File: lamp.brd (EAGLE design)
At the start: 127.3 x 38.1 mm, 53 parts

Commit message: Fiddled the board xml by hand to place the last few parts. Some more adjustment of traces. Added a low-noise cap to the 5v regulator.
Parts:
- added C3: 10nF, Barebones-Arduino:0805
- C1: value (none) -> 1µF
- C2: value (none) -> 2.2µF
- moved C2 1.62 mm to (67.3, 4.13), turned to 180 degrees
- moved C1 1.27 mm to (58.7, 5.71)
- moved LR 1.27 mm to (62.2, 5.71)
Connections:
- new net N$46: C3.1, LR.P$4
- net GND: now also C3.2
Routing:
- net N$15: track 14.1 -> 22.4 mm
- net N$46: track 0.00 -> 2.99 mm
- net GND: vias 8 -> 10
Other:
- board text added: "C1"
- board text added: "C2"
- board text added: "C3"
- board text added: "LR"
- board text added: "R1"
- board text added: "R10"
- board text added: "R2"
- board text added: "R3"
- board text added: "R4"
- board text added: "R5"
- board text added: "R6"
- board text added: "R7"
- board text added: "R8"
- board text added: "R9"
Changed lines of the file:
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@@
 <rectangle x1="120.9675" y1="30.1625" x2="124.46" y2="32.7025" layer="1"/>
 <rectangle x1="120.9675" y1="33.3375" x2="124.46" y2="35.8775" layer="1"/>
+<text x="62.23" y="3.81" size="1.016" layer="26" rot="MR0" align="top-center">LR</text>
+<text x="57.785" y="5.715" size="1.016" layer="26" rot="MR0" align="center-left">C1</text>
+<text x="69.215" y="6.35" size="1.016" layer="26" rot="MR0" align="center-right">C3</text>
+<text x="69.215" y="4.1275" size="1.016" layer="26" rot="MR0" align="center-right">C2</text>
+<text x="10.795" y="34.925" size="1.016" layer="26" rot="MR180" align="top-center">R10</text>
+<text x="23.495" y="34.925" size="1.016" layer="26" rot="MR180" align="top-center">R9</text>
+<text x="36.195" y="34.925" size="1.016" layer="26" rot="MR180" align="top-center">R8</text>
+<text x="48.895" y="34.925" size="1.016" layer="26" rot="MR180" align="top-center">R7</text>
+<text x="61.595" y="34.925" size="1.016" layer="26" rot="MR180" align="top-center">R6</text>
+<text x="65.405" y="34.925" size="1.016" layer="26" rot="MR180" align="top-center">R5</text>
+<text x="78.105" y="34.925" size="1.016" layer="26" rot="MR180" align="top-center">R4</text>
+<text x="90.805" y="34.925" size="1.016" layer="26" rot="MR180" align="top-center">R3</text>
+<text x="103.505" y="34.925" size="1.016" layer="26" rot="MR180" align="top-center">R2</text>
+<text x="116.205" y="34.925" size="1.016" layer="26" rot="MR180" align="top-center">R1</text>
 </plain>
 <attributes>
@@
 <element name="U$17" library="lamp" package="PLCC4" value="CLA1BWKWMKW-4" x="57.15" y="19.05" rot="R90"/>
 <element name="U$18" library="lamp" package="PLCC4" value="CLA1BWKWMKW-4" x="57.15" y="33.02" rot="R90"/>
-<element name="LR" library="lamp" package="SOT-23-5" value="LP2985" x="63.5" y="5.715" smashed="yes" rot="MR90"/>
-<element name="C1" library=" Barebones-Arduino" package="0805" value="" x="60.0075" y="5.715" rot="MR90"/>
-<element name="C2" library=" Barebones-Arduino" package="0805" value="" x="66.9925" y="5.715" rot="MR90"/>
+<element name="LR" library="lamp" package="SOT-23-5" value="LP2985" x="62.23" y="5.715" smashed="yes" rot="MR90"/>
+<element name="C1" library=" Barebones-Arduino" package="0805" value="1µF" x="58.7375" y="5.715" rot="MR90"/>
+<element name="C2" library=" Barebones-Arduino" package="0805" value="2.2µF" x="67.31" y="4.1275" rot="MR180"/>
 <element name="PB1" library="wirepad" package="SMD1,27-2,54" value="" x="73.3425" y="11.7475" smashed="yes" rot="MR270">
 <attribute name="VALUE" x="73.3425" y="11.7475" size="0.0254" layer="28" rot="MR270"/>
@@
 <attribute name="NAME" x="51.6125" y="13.1825" size="1.27" layer="26" rot="MR0"/>
 </element>
+<element name="C3" library=" Barebones-Arduino" package="0805" value="10nF" x="67.31" y="6.35" rot="MR180"/>
 </elements>
 <signals>
@@
 <contactref element="LR" pad="P$1"/>
 <via x="63.5" y="1.27" extent="1-16" drill="0.5"/>
-<wire x1="63.5" y1="4.7625" x2="63.5" y2="6.0325" width="0.4064" layer="16"/>
-<wire x1="63.5" y1="6.0325" x2="62.865" y2="6.6675" width="0.4064" layer="16"/>
-<wire x1="62.865" y1="6.6675" x2="62.23" y2="6.6675" width="0.4064" layer="16"/>
-<wire x1="63.5" y1="1.27" x2="63.5" y2="4.7625" width="0.4064" layer="16"/>
-<wire x1="63.5" y1="4.7625" x2="60.0075" y2="4.7625" width="0.4064" layer="16"/>
+<wire x1="62.23" y1="4.7625" x2="62.23" y2="6.0325" width="0.4064" layer="16"/>
+<wire x1="62.23" y1="6.0325" x2="61.595" y2="6.6675" width="0.4064" layer="16"/>
+<wire x1="61.595" y1="6.6675" x2="60.96" y2="6.6675" width="0.4064" layer="16"/>
+<wire x1="63.5" y1="1.27" x2="62.23" y2="4.7625" width="0.4064" layer="16"/>
+<wire x1="62.23" y1="4.7625" x2="58.7375" y2="4.7625" width="0.4064" layer="16"/>
 <wire x1="121.6025" y1="1.27" x2="121.6025" y2="4.1275" width="1.27" layer="1"/>
 <wire x1="108.9025" y1="4.1275" x2="108.9025" y2="1.5875" width="1.27" layer="1"/>
 <wire x1="83.5025" y1="40.9575" x2="96.2025" y2="40.9575" width="0" layer="19" extent="1-1"/>
 <wire x1="63.5" y1="22.86" x2="83.5025" y2="40.9575" width="0" layer="19" extent="1-16"/>
-<wire x1="62.18" y1="6.635" x2="62.23" y2="6.6675" width="0" layer="19" extent="16-16"/>
-<wire x1="60.0075" y1="4.865" x2="60.0075" y2="4.7625" width="0" layer="19" extent="16-16"/>
-<wire x1="62.18" y1="4.795" x2="63.5" y2="4.7625" width="0" layer="19" extent="16-16"/>
+<wire x1="60.91" y1="6.635" x2="60.96" y2="6.6675" width="0" layer="19" extent="16-16"/>
+<wire x1="58.7375" y1="4.865" x2="58.7375" y2="4.7625" width="0" layer="19" extent="16-16"/>
+<wire x1="60.91" y1="4.795" x2="62.23" y2="4.7625" width="0" layer="19" extent="16-16"/>
 <wire x1="108.9025" y1="4.1275" x2="121.6025" y2="4.1275" width="0" layer="19" extent="1-1"/>
 <wire x1="96.2025" y1="3.4925" x2="83.5025" y2="3.4925" width="0" layer="19" extent="1-1"/>
@@
 <vertex x="127" y="0"/>
 </polygon>
-<wire x1="60.0075" y1="6.35" x2="60.96" y2="6.35" width="0.4064" layer="16"/>
-<wire x1="60.96" y1="6.35" x2="61.2775" y2="5.715" width="0.4064" layer="16"/>
-<wire x1="61.2775" y1="5.715" x2="62.23" y2="5.715" width="0.4064" layer="16"/>
-<polygon width="0" layer="1" spacing="0.254">
+<wire x1="58.7375" y1="6.35" x2="59.69" y2="6.35" width="0.4064" layer="16"/>
+<wire x1="59.69" y1="6.35" x2="60.0075" y2="5.715" width="0.4064" layer="16"/>
+<wire x1="60.0075" y1="5.715" x2="60.96" y2="5.715" width="0.4064" layer="16"/>
+<polygon width="0" layer="1" spacing="0.254" isolate="0.4064">
 <vertex x="0" y="0"/>
 <vertex x="127" y="0"/>
@@
 <via x="101.6" y="19.05" extent="1-16" drill="0.5"/>
 <via x="114.3" y="19.05" extent="1-16" drill="0.5"/>
+<contactref element="C3" pad="2"/>
+<via x="1.905" y="19.05" extent="1-16" drill="0.5"/>
+<via x="125.4125" y="19.05" extent="1-16" drill="0.5"/>
 </signal>
 <signal name="N$14">
@@
 </signal>
 <signal name="N$15">
-<wire x1="64.77" y1="4.7625" x2="68.58" y2="4.7625" width="0.4064" layer="16"/>
+<wire x1="66.675" y1="2.8575" x2="73.3425" y2="2.8575" width="0.4064" layer="16"/>
 <contactref element="LR" pad="P$5"/>
 <contactref element="C2" pad="1"/>
@@
 <wire x1="67.31" y1="8.89" x2="68.58" y2="8.89" width="0.4064" layer="16"/>
 <wire x1="68.58" y1="8.89" x2="73.3425" y2="7.9375" width="0.4064" layer="16"/>
-<wire x1="68.58" y1="4.7625" x2="68.58" y2="8.89" width="0.4064" layer="16"/>
-<wire x1="68.58" y1="4.7625" x2="66.9925" y2="4.865" width="0" layer="19" extent="16-16"/>
-<wire x1="64.87" y1="4.795" x2="64.77" y2="4.7625" width="0" layer="19" extent="16-16"/>
+<wire x1="73.3425" y1="2.8575" x2="73.3425" y2="7.9375" width="0.4064" layer="16"/>
+<wire x1="66.675" y1="2.8575" x2="66.3575" y2="3.175" width="0.4064" layer="16"/>
+<wire x1="66.3575" y1="3.175" x2="66.3575" y2="4.1275" width="0.4064" layer="16"/>
+<wire x1="66.3575" y1="4.1275" x2="65.405" y2="4.1275" width="0.4064" layer="16"/>
+<wire x1="65.405" y1="4.1275" x2="64.77" y2="4.7625" width="0.4064" layer="16"/>
+<wire x1="64.77" y1="4.7625" x2="63.5" y2="4.7625" width="0.4064" layer="16"/>
+<wire x1="66.3575" y1="4.1275" x2="66.46" y2="4.1275" width="0" layer="19" extent="16-16"/>
+<wire x1="63.6" y1="4.795" x2="63.5" y2="4.7625" width="0" layer="19" extent="16-16"/>
 </signal>
 <signal name="N$49">
@@
 <wire x1="119.6975" y1="35.2425" x2="119.6975" y2="33.9725" width="1.27" layer="1"/>
 </signal>
+<signal name="N$46">
+<contactref element="LR" pad="P$4"/>
+<contactref element="C3" pad="1"/>
+<wire x1="63.5" y1="6.6675" x2="64.77" y2="6.6675" width="0.4064" layer="16"/>
+<wire x1="64.77" y1="6.6675" x2="65.0875" y2="6.35" width="0.4064" layer="16"/>
+<wire x1="65.0875" y1="6.35" x2="66.3575" y2="6.35" width="0.4064" layer="16"/>
+<wire x1="66.3575" y1="6.35" x2="66.46" y2="6.35" width="0" layer="19" extent="16-16"/>
+<wire x1="63.6" y1="6.635" x2="63.5" y2="6.6675" width="0" layer="19" extent="16-16"/>
+</signal>
 </signals>

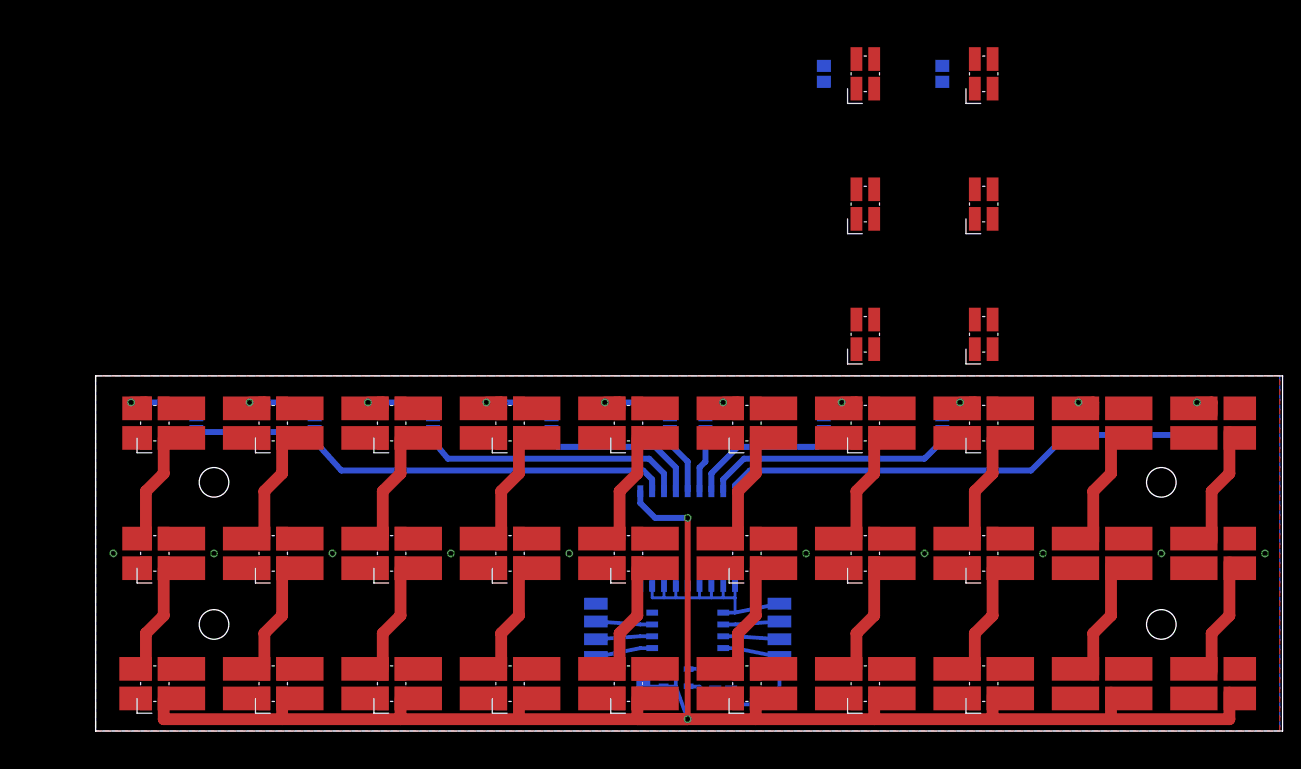
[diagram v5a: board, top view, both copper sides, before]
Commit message: More fiddling: moved some parts around, started adding capacitive touch on/off switch
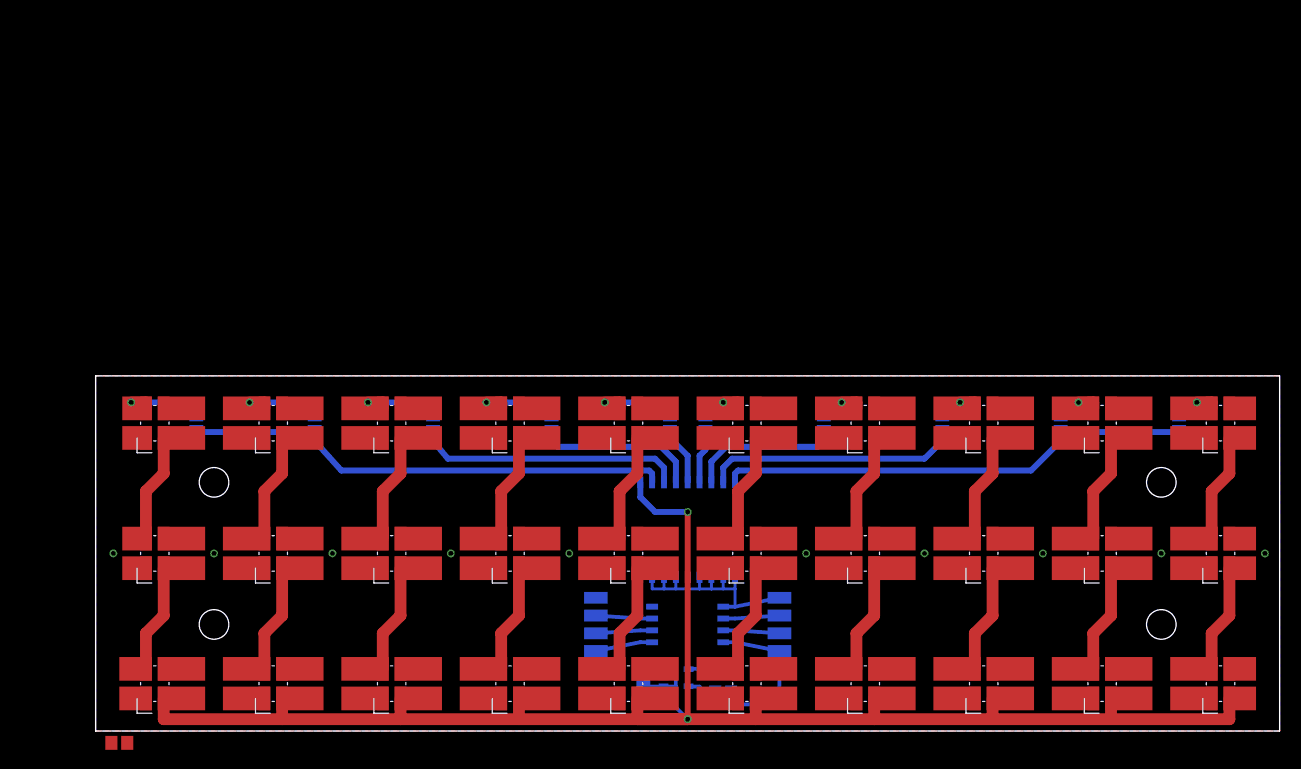
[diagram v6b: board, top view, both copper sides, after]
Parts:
- added R11: 1MΩ, Barebones-Arduino:0805
- moved U$2 53.4 mm to (120.7, 5.08)
- moved U$3 53.4 mm to (120.7, 19.1)
- moved U$4 53.4 mm to (120.7, 33.0)
- moved R1 53.4 mm to (116.2, 33.0)
- moved U$5 39.6 mm to (108.0, 5.08)
- moved U$6 39.6 mm to (108.0, 19.1)
- moved U$7 39.6 mm to (108.0, 33.0)
- moved R2 39.6 mm to (103.5, 33.0)
- moved TA 0.95 mm to (63.5, 21.6)
- moved GND 0.63 mm to (53.7, 14.3)
- moved PB0 0.63 mm to (73.3, 14.3)
- moved PB1 0.63 mm to (73.3, 12.4)
- moved PB2 0.63 mm to (73.3, 10.5)
- moved PB3 0.63 mm to (53.7, 10.5)
- moved PB4 0.63 mm to (53.7, 12.4)
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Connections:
- new net +5V: UC.P$8, VCC.1
- net N$14: now also R11.2
- net N$15: no longer UC.P$8, VCC.1
- net N$17: now also R11.1
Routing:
- net +5V: track 0.00 -> 23.0 mm
- net N$15: track 22.4 -> 0.00 mm
- net N$50: track 12.5 -> 0.00 mm
- net N$53: track 12.5 -> 0.00 mm
- net N$49: track 12.5 -> 0.00 mm
- net N$54: track 12.2 -> 0.00 mm
- net N$6: track 0.00 -> 11.6 mm
- net N$3: track 0.00 -> 11.6 mm
- net N$4: track 0.00 -> 11.6 mm
- net N$1: track 0.00 -> 11.6 mm
- net N$51: track 5.29 -> 0.00 mm, vias 1 -> 0
- net N$45: track 5.29 -> 0.00 mm, vias 1 -> 0
- net N$2: track 0.00 -> 4.65 mm, vias 0 -> 1
- net N$5: track 0.00 -> 4.65 mm, vias 0 -> 1
- net N$42: track 6.61 -> 5.66 mm
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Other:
- board size 127.3 x 38.1 mm -> 127 x 38.1 mm

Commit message: Fixed some footprints, mangled some others, and added a temporary placeholder for the header block that will be for power and the switch.
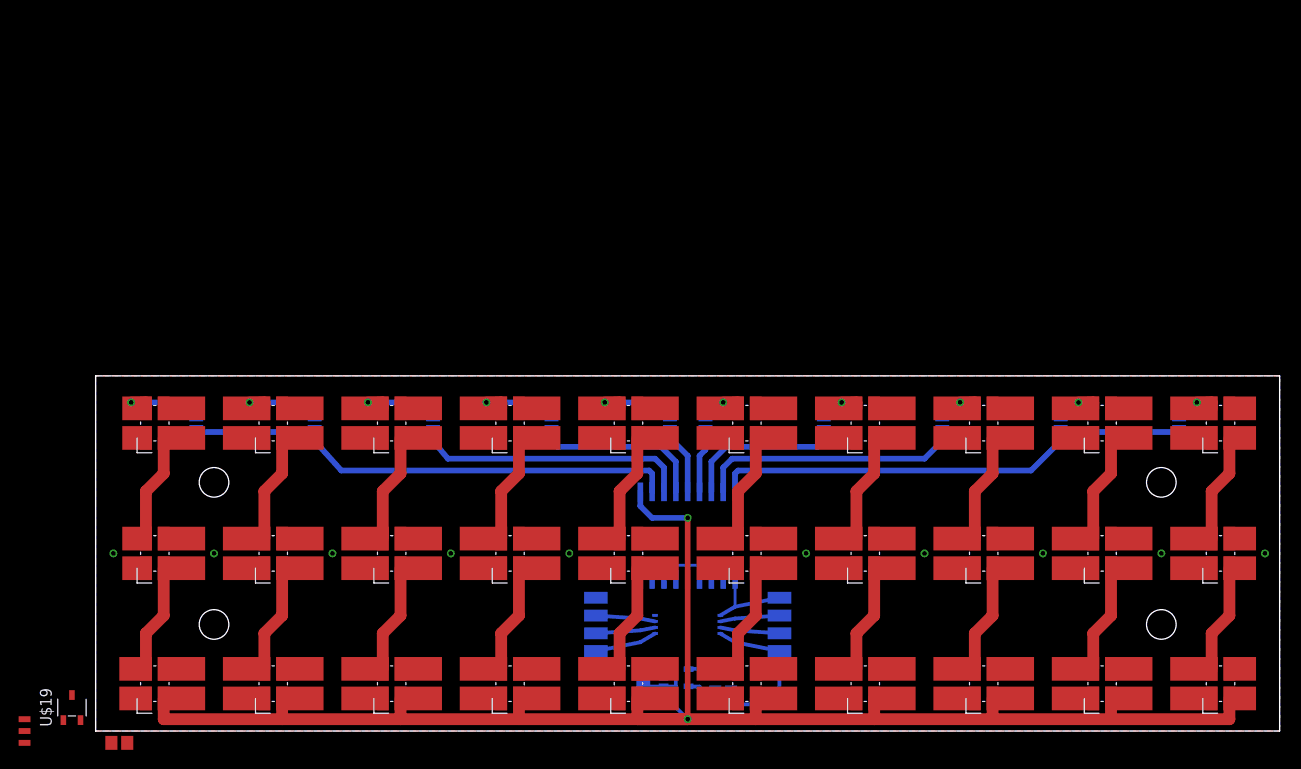
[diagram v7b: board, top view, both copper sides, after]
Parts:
- added U$19: SI2319DS, lamp:SOT-23-3
- added U$32: HEADER-3X1, lamp:HEADER-3X1
- moved TA 0.64 mm to (63.5, 21.0)
- renumbered LR to VR
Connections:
- new net N$45: C1.1, U$19.P$2, VR.P$1, VR.P$3
- net +12V: now also U$19.P$3, U$32.P$1; no longer C1.1, VR.P$1, VR.P$3
- net GND: now also U$19.P$1, U$32.P$3
- net N$17: now also U$32.P$2
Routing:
- net N$47: track 27.1 -> 30.7 mm
- net N$42: track 5.66 -> 6.68 mm
- net N$41: track 6.19 -> 7.20 mm
- net N$38: track 51.0 -> 52.0 mm
- net N$37: track 27.2 -> 28.2 mm
- net N$36: track 16.2 -> 17.2 mm
- net N$35: track 52.3 -> 53.4 mm
- net N$34: track 28.6 -> 29.6 mm
- net N$33: track 17.4 -> 18.4 mm
- net +12V: track 179.2 -> 178.4 mm
- net +5V: track 23.0 -> 23.6 mm
- net N$18: track 6.13 -> 6.69 mm
